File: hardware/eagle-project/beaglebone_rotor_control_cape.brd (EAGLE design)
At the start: 71.8 x 54.6 mm, 21 parts, among them IC1 TLC2264CDU, IC2 TLV5616, IC3 MAX3232ESE, Q1 SQ2348ES-T1-GE3, Q2 SQ2348ES-T1-GE3, X1 BEAGLEBONE_OUTLINE

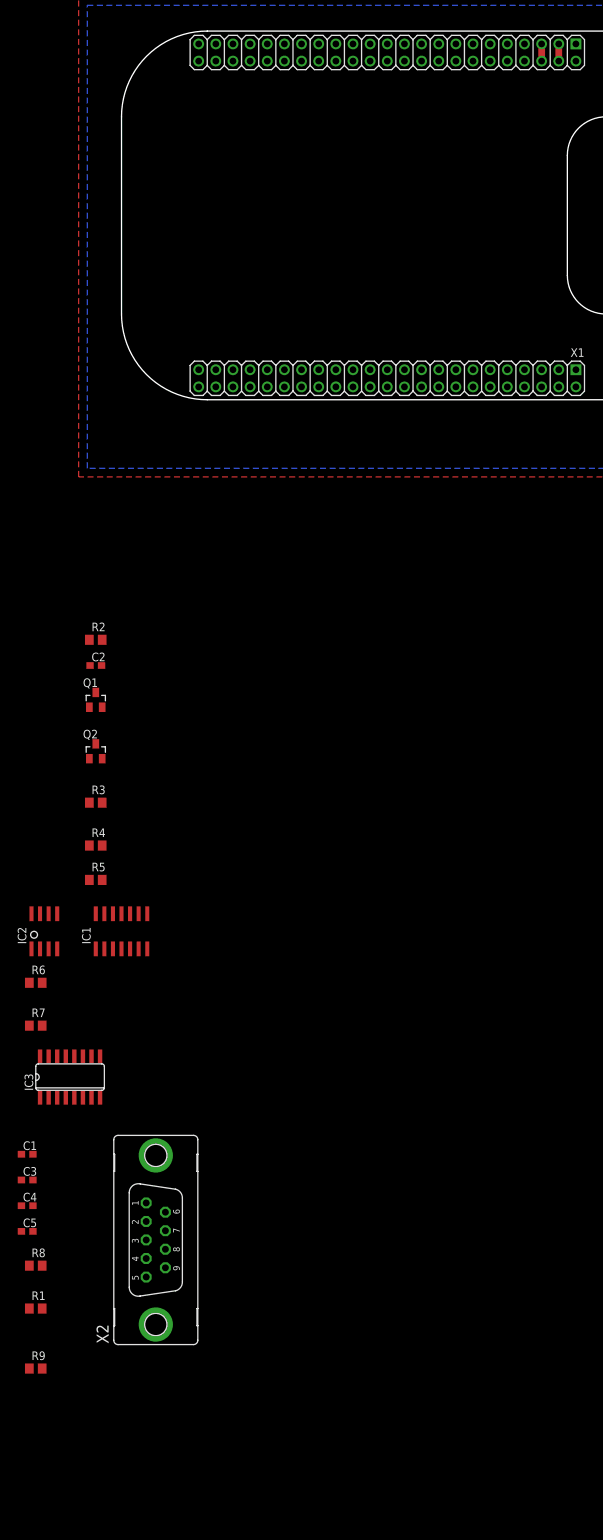
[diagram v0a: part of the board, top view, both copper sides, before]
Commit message: Eagle project update * RS232 rcv/drv layout done * AMP Press-Fit connector library created
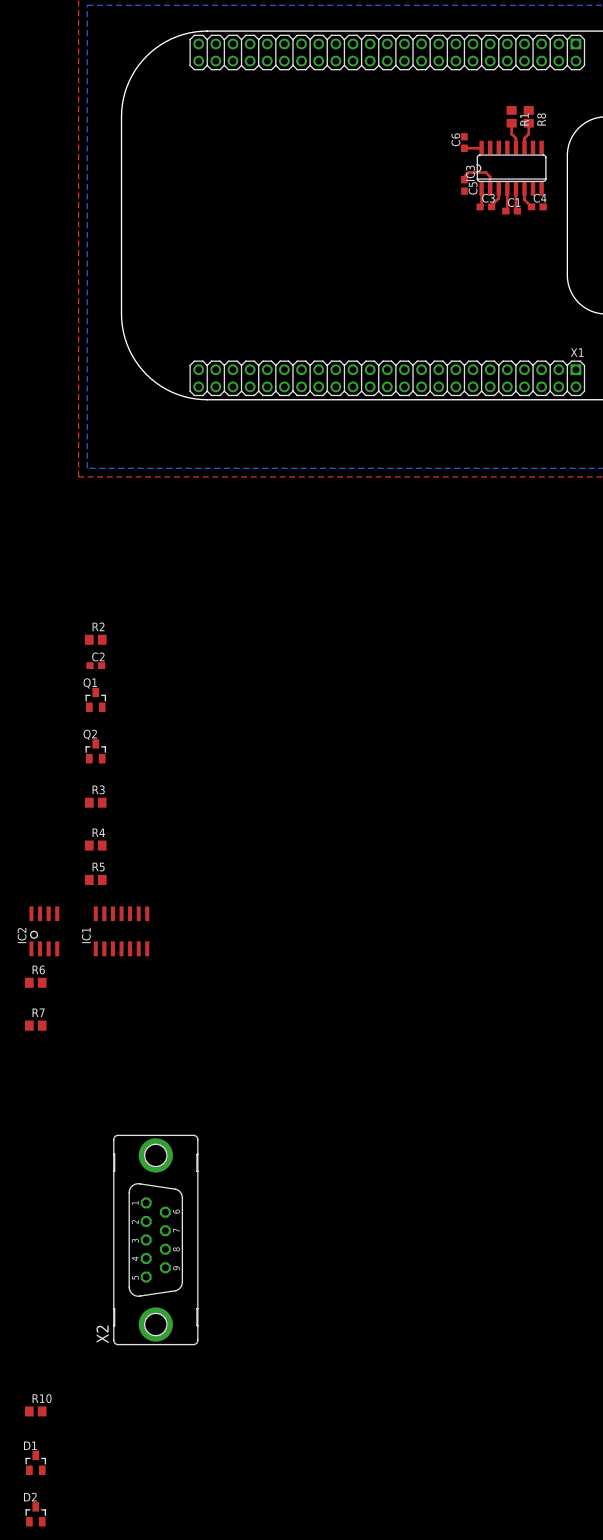
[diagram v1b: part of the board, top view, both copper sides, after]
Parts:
- removed R9: 15k, rcl:R0805
- added C6: 100n, rcl:C0603
- added D1: BAS40-04, diode:SOT23
- added D2: 5V1, diode:SOT23
- added R10: 10k, rcl:R0805
- R4: value (none) -> 10k
- R5: value (none) -> 5k6
- moved R1 190.1 mm to (59.1, 43.2), turned to 270 degrees
- moved R8 185.2 mm to (61.6, 43.2), turned to 270 degrees
- moved C5 167.9 mm to (52.1, 33.0), turned to 270 degrees
- moved C4 166.1 mm to (62.9, 29.8)
- moved C3 159.4 mm to (55.2, 29.8)
- moved C1 157.1 mm to (59.1, 29.2)
- moved IC3 149.7 mm to (59.1, 35.6)
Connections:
- removed net N$23: R1.1
- removed net N$24: R8.1
- removed net N$26: IC3.14
- removed net N$27: IC3.13
- removed net VCC: IC3.16
- removed net VDD_3V3EXP: X1.49, X1.50
- removed net VDD_5V: X1.51, X1.52
- new net +3V3: C6.1, IC3.16, X1.49, X1.50
- new net BB_UART4_RX: R1.1, X1.57
- new net BB_UART4_TX: R8.1, X1.59
- new net N$28: R10.2
- new net RS232_RX: IC3.13, X2.3
- new net RS232_TX: IC3.14, X2.2
- net +5V: now also D1.2, X1.51, X1.52
- net GND: now also C6.2, D1.1, D2.1, X2.5; no longer R9.1
- net N$12: now also D1.3, D2.3, R10.1; no longer R9.2
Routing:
- net N$21: track 0.00 -> 6.56 mm
- net N$25: track 0.00 -> 3.86 mm
- net N$22: track 0.00 -> 3.86 mm
- net N$17: track 0.00 -> 3.37 mm
- net N$16: track 0.00 -> 3.37 mm
- net N$20: track 0.00 -> 3.08 mm
- net N$18: track 0.00 -> 3.08 mm
- net N$19: track 0.00 -> 2.73 mm
- net +3V3: track 0.00 -> 2.59 mm
- net VDD_5V: track 2.54 -> 0.00 mm
- net VDD_3V3EXP: track 2.54 -> 0.00 mm

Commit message: Updated available components list
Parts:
- added C7: 100n, rcl:C0603
- added R9: 100, rcl:R0805
- C2: value (none) -> 100n
- moved R6 98.4 mm to (-12.1, -183.5)
- moved R7 85.7 mm to (-12.1, -177.2)
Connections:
- net N$28 renamed ROT_H_POSITON
- net N$3 renamed ROT_H_LEFT
- net N$6 renamed ROT_H_RIGHT
- removed net N$10: IC2.6
- new net ROT_H_SPEED: R9.2
- net +5V: now also C7.1, IC2.6
- net GND: now also C7.2
- net N$11: now also R7.2; no longer R7.1
- net N$13: now also R6.2; no longer R6.1
- net N$14: now also R7.1; no longer R7.2
- net N$15: now also R6.1; no longer R6.2
- net N$5: now also R9.1
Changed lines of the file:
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@@
 <elements>
 <element name="X1" library="beaglebone" package="BEAGLEBONE_SHIELD" value="BEAGLEBONE_OUTLINE" x="87.63" y="1.27" rot="R90"/>
-<element name="C2" library="rcl" package="C0603" value="" x="-2.54" y="-38.1"/>
+<element name="C2" library="rcl" package="C0603" value="100n" x="-2.54" y="-38.1"/>
 <element name="R2" library="rcl" package="R0805" value="1M" x="-2.54" y="-34.29"/>
 <element name="Q1" library="vishay_sq2348eS-t1-ge3" package="SOT23" value="SQ2348ES-T1-GE3" x="-2.54" y="-43.18"/>
@@
 <element name="IC1" library="ti-tlc2264cd" package="SO14" value="TLC2264CDU" x="1.27" y="-77.47"/>
 <element name="IC2" library="ti-tlv5616" package="SO08" value="TLV5616" x="-10.16" y="-77.47"/>
-<element name="R6" library="rcl" package="R0805" value="100" x="-11.43" y="-85.09"/>
-<element name="R7" library="rcl" package="R0805" value="100" x="-11.43" y="-91.44"/>
 <element name="IC3" library="maxim" package="SO16" value="MAX3232ESE" x="59.055" y="35.56">
 <attribute name="OC_NEWARK" value="79C3880" x="59.055" y="35.56" size="1.778" layer="27" display="off"/>
@@
 <element name="D2" library="diode" package="SOT23" value="5V1" x="-11.43" y="-163.83"/>
 <element name="C6" library="rcl" package="C0603" value="100n" x="52.07" y="39.37" rot="R90"/>
+<element name="R9" library="rcl" package="R0805" value="100" x="-12.065" y="-170.815"/>
+<element name="R7" library="rcl" package="R0805" value="100" x="-12.065" y="-177.165"/>
+<element name="R6" library="rcl" package="R0805" value="100" x="-12.065" y="-183.515"/>
+<element name="C7" library="rcl" package="C0603" value="100n" x="-12.7" y="-189.23"/>
 </elements>
 <signals>
@@
 <contactref element="C6" pad="2"/>
 <contactref element="X2" pad="5"/>
+<contactref element="C7" pad="2"/>
+<wire x1="-12.38" y1="-164.93" x2="-11.85" y2="-189.23" width="0" layer="19" extent="1-1"/>
 <wire x1="-12.38" y1="-157.31" x2="-12.38" y2="-164.93" width="0" layer="19" extent="1-1"/>
 <wire x1="4.9276" y1="-128.6764" x2="-12.38" y2="-157.31" width="0" layer="19" extent="1-1"/>
@@
 <wire x1="-3.49" y1="-34.29" x2="-1.69" y2="-38.1" width="0" layer="19" extent="1-1"/>
 <wire x1="68.58" y1="3.175" x2="-3.49" y2="-34.29" width="0" layer="19" extent="1-1"/>
-</signal>
-<signal name="N$3">
+<wire x1="68.58" y1="5.715" x2="68.58" y2="3.175" width="0" layer="19" extent="1-1"/>
+<wire x1="63.715" y1="29.845" x2="68.58" y2="5.715" width="0" layer="19" extent="1-1"/>
+<wire x1="55.88" y1="38.6334" x2="63.715" y2="29.845" width="0" layer="19" extent="1-1"/>
+<wire x1="52.07" y1="40.22" x2="55.88" y2="38.6334" width="0" layer="19" extent="1-1"/>
+<wire x1="52.07" y1="32.17" x2="55.88" y2="38.6334" width="0" layer="19" extent="1-1"/>
+<wire x1="68.58" y1="51.435" x2="55.88" y2="38.6334" width="0" layer="19" extent="1-1"/>
+<wire x1="68.58" y1="53.975" x2="68.58" y2="51.435" width="0" layer="19" extent="1-1"/>
+<wire x1="15.24" y1="51.435" x2="52.07" y2="40.22" width="0" layer="19" extent="1-1"/>
+<wire x1="15.24" y1="53.975" x2="15.24" y2="51.435" width="0" layer="19" extent="1-1"/>
+<wire x1="12.7" y1="53.975" x2="15.24" y2="53.975" width="0" layer="19" extent="1-1"/>
+<wire x1="12.7" y1="51.435" x2="15.24" y2="51.435" width="0" layer="19" extent="1-1"/>
+</signal>
+<signal name="ROT_H_LEFT">
 <contactref element="Q1" pad="3"/>
 </signal>
-<signal name="N$6">
+<signal name="ROT_H_RIGHT">
 <contactref element="Q2" pad="3"/>
 </signal>
@@
 <contactref element="X1" pad="51"/>
 <contactref element="X1" pad="52"/>
+<contactref element="C7" pad="1"/>
+<contactref element="IC2" pad="6"/>
+<wire x1="-10.48" y1="-157.31" x2="-13.55" y2="-189.23" width="0" layer="19" extent="1-1"/>
 <wire x1="1.27" y1="-80.07" x2="-10.48" y2="-157.31" width="0" layer="19" extent="1-1"/>
-<wire x1="-12.065" y1="-74.87" x2="1.27" y2="-80.07" width="0" layer="19" extent="1-1"/>
+<wire x1="-9.525" y1="-74.87" x2="1.27" y2="-80.07" width="0" layer="19" extent="1-1"/>
+<wire x1="-12.065" y1="-74.87" x2="-9.525" y2="-74.87" width="0" layer="19" extent="1-1"/>
 <wire x1="63.5" y1="51.435" x2="1.27" y2="-80.07" width="0" layer="19" extent="1-1"/>
 <wire x1="63.5" y1="53.975" x2="63.5" y2="51.435" width="0" layer="19" extent="1-1"/>
@@
 <contactref element="IC1" pad="1"/>
 <contactref element="IC1" pad="2"/>
+<contactref element="R9" pad="1"/>
+<wire x1="-2.54" y1="-80.07" x2="-13.015" y2="-170.815" width="0" layer="19" extent="1-1"/>
 <wire x1="-1.27" y1="-80.07" x2="-2.54" y2="-80.07" width="0" layer="19" extent="1-1"/>
 </signal>
@@
 <signal name="N$9">
 <contactref element="IC2" pad="4"/>
-</signal>
-<signal name="N$10">
-<contactref element="IC2" pad="6"/>
 </signal>
 <signal name="N$12">
@@
 <contactref element="R3" pad="2"/>
 <contactref element="Q2" pad="1"/>
-<contactref element="R7" pad="1"/>
-<wire x1="-1.59" y1="-58.42" x2="-12.38" y2="-91.44" width="0" layer="19" extent="1-1"/>
+<contactref element="R7" pad="2"/>
+<wire x1="-1.59" y1="-58.42" x2="-11.115" y2="-177.165" width="0" layer="19" extent="1-1"/>
 <wire x1="-3.49" y1="-51.9" x2="-1.59" y2="-58.42" width="0" layer="19" extent="1-1"/>
 </signal>
@@
 <contactref element="R2" pad="2"/>
 <contactref element="Q1" pad="1"/>
-<contactref element="R6" pad="1"/>
-<wire x1="-3.49" y1="-44.28" x2="-12.38" y2="-85.09" width="0" layer="19" extent="1-1"/>
+<contactref element="R6" pad="2"/>
+<wire x1="-3.49" y1="-44.28" x2="-11.115" y2="-183.515" width="0" layer="19" extent="1-1"/>
 <wire x1="-1.59" y1="-34.29" x2="-3.49" y2="-44.28" width="0" layer="19" extent="1-1"/>
-</signal>
-<signal name="N$14">
-<contactref element="R7" pad="2"/>
-</signal>
-<signal name="N$15">
-<contactref element="R6" pad="2"/>
 </signal>
 <signal name="N$16">
@@
 <wire x1="58.42" y1="38.6334" x2="4.9276" y2="-123.19" width="0" layer="19" extent="1-1"/>
 </signal>
-<signal name="N$28">
+<signal name="ROT_H_POSITON">
 <contactref element="R10" pad="2"/>
 </signal>
@@
 <wire x1="61.595" y1="44.13" x2="53.34" y2="53.975" width="0" layer="19" extent="1-1"/>
 </signal>
+<signal name="ROT_H_SPEED">
+<contactref element="R9" pad="2"/>
+</signal>
+<signal name="N$14">
+<contactref element="R7" pad="1"/>
+</signal>
+<signal name="N$15">
+<contactref element="R6" pad="1"/>
+</signal>
 </signals>

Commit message: Changed DAC from TI TLV5616 to Microchip MCP4901
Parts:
- IC2: value TLV5616 -> MCP4901; device ti-tlv5616:SO08 -> microchip_mcp4901:SO-08
- moved IC2 110.1 mm to (-17.8, -187.3)
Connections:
- removed net N$8: IC2.1
- new net N$7: IC2.5
- net +5V: now also IC2.1; no longer IC2.8
- net GND: now also IC2.7; no longer IC2.5
- net N$2: now also IC2.8; no longer IC2.7
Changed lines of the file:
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@@
 <element name="R5" library="rcl" package="R0805" value="5k6" x="-2.54" y="-69.85"/>
 <element name="IC1" library="ti-tlc2264cd" package="SO14" value="TLC2264CDU" x="1.27" y="-77.47"/>
-<element name="IC2" library="ti-tlv5616" package="SO08" value="TLV5616" x="-10.16" y="-77.47"/>
 <element name="IC3" library="maxim" package="SO16" value="MAX3232ESE" x="59.055" y="35.56">
 <attribute name="OC_NEWARK" value="79C3880" x="59.055" y="35.56" size="1.778" layer="27" display="off"/>
@@
 <element name="R6" library="rcl" package="R0805" value="100" x="-12.065" y="-183.515"/>
 <element name="C7" library="rcl" package="C0603" value="100n" x="-12.7" y="-189.23"/>
+<element name="IC2" library="microchip_mcp4901" package="SO-08" value="MCP4901" x="-17.78" y="-187.325"/>
 </elements>
 <signals>
@@
 <contactref element="C2" pad="2"/>
 <contactref element="IC1" pad="11"/>
-<contactref element="IC2" pad="5"/>
 <contactref element="IC3" pad="15"/>
 <contactref element="C4" pad="2"/>
@@
 <contactref element="X2" pad="5"/>
 <contactref element="C7" pad="2"/>
-<wire x1="-12.38" y1="-164.93" x2="-11.85" y2="-189.23" width="0" layer="19" extent="1-1"/>
+<contactref element="IC2" pad="7"/>
+<wire x1="-11.85" y1="-189.23" x2="-18.415" y2="-184.725" width="0" layer="19" extent="1-1"/>
+<wire x1="-12.38" y1="-164.93" x2="-18.415" y2="-184.725" width="0" layer="19" extent="1-1"/>
 <wire x1="-12.38" y1="-157.31" x2="-12.38" y2="-164.93" width="0" layer="19" extent="1-1"/>
 <wire x1="4.9276" y1="-128.6764" x2="-12.38" y2="-157.31" width="0" layer="19" extent="1-1"/>
 <wire x1="1.27" y1="-74.87" x2="4.9276" y2="-128.6764" width="0" layer="19" extent="1-1"/>
 <wire x1="-3.49" y1="-69.85" x2="1.27" y2="-74.87" width="0" layer="19" extent="1-1"/>
-<wire x1="-8.255" y1="-74.87" x2="-3.49" y2="-69.85" width="0" layer="19" extent="1-1"/>
 <wire x1="-3.49" y1="-58.42" x2="-3.49" y2="-69.85" width="0" layer="19" extent="1-1"/>
 <wire x1="-1.59" y1="-51.9" x2="-3.49" y2="-58.42" width="0" layer="19" extent="1-1"/>
@@
 <signal name="+5V">
 <contactref element="IC1" pad="4"/>
-<contactref element="IC2" pad="8"/>
 <contactref element="D1" pad="2"/>
 <contactref element="X1" pad="51"/>
 <contactref element="X1" pad="52"/>
 <contactref element="C7" pad="1"/>
+<contactref element="IC2" pad="1"/>
 <contactref element="IC2" pad="6"/>
-<wire x1="-10.48" y1="-157.31" x2="-13.55" y2="-189.23" width="0" layer="19" extent="1-1"/>
+<wire x1="-17.145" y1="-184.725" x2="-19.685" y2="-189.925" width="0" layer="19" extent="1-1"/>
+<wire x1="-13.55" y1="-189.23" x2="-17.145" y2="-184.725" width="0" layer="19" extent="1-1"/>
+<wire x1="-10.48" y1="-157.31" x2="-17.145" y2="-184.725" width="0" layer="19" extent="1-1"/>
 <wire x1="1.27" y1="-80.07" x2="-10.48" y2="-157.31" width="0" layer="19" extent="1-1"/>
-<wire x1="-9.525" y1="-74.87" x2="1.27" y2="-80.07" width="0" layer="19" extent="1-1"/>
-<wire x1="-12.065" y1="-74.87" x2="-9.525" y2="-74.87" width="0" layer="19" extent="1-1"/>
 <wire x1="63.5" y1="51.435" x2="1.27" y2="-80.07" width="0" layer="19" extent="1-1"/>
 <wire x1="63.5" y1="53.975" x2="63.5" y2="51.435" width="0" layer="19" extent="1-1"/>
@@
 </signal>
 <signal name="N$2">
-<contactref element="IC2" pad="7"/>
 <contactref element="IC1" pad="3"/>
-<wire x1="0" y1="-80.07" x2="-10.795" y2="-74.87" width="0" layer="19" extent="1-1"/>
-</signal>
-<signal name="N$4">
-<contactref element="IC2" pad="3"/>
-</signal>
-<signal name="N$7">
-<contactref element="IC2" pad="2"/>
-</signal>
-<signal name="N$8">
-<contactref element="IC2" pad="1"/>
-</signal>
-<signal name="N$9">
-<contactref element="IC2" pad="4"/>
+<contactref element="IC2" pad="8"/>
+<wire x1="0" y1="-80.07" x2="-19.685" y2="-184.725" width="0" layer="19" extent="1-1"/>
 </signal>
 <signal name="N$12">
@@
 <contactref element="R6" pad="1"/>
 </signal>
+<signal name="N$3">
+<contactref element="IC2" pad="2"/>
+</signal>
+<signal name="N$4">
+<contactref element="IC2" pad="3"/>
+</signal>
+<signal name="N$6">
+<contactref element="IC2" pad="4"/>
+</signal>
+<signal name="N$7">
+<contactref element="IC2" pad="5"/>
+</signal>
 </signals>

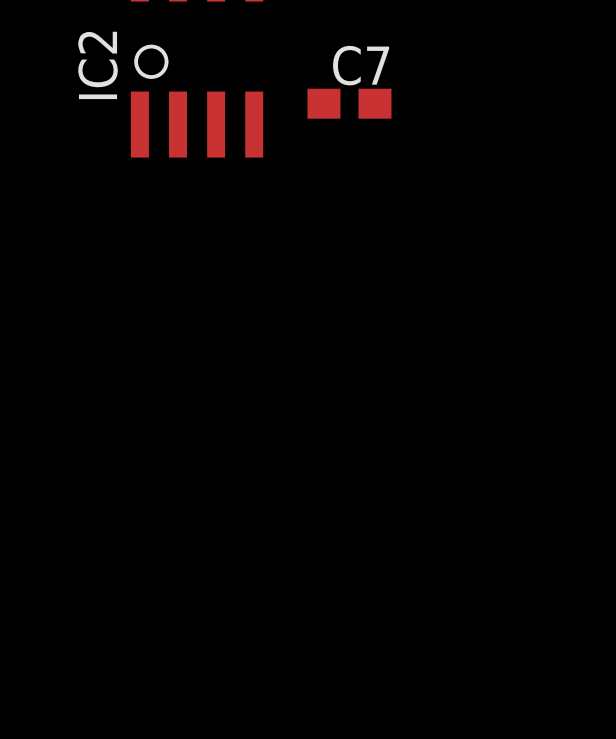
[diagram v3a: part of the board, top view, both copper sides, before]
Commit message: Added software draft for MCP4901 and some Eagle schematic updates
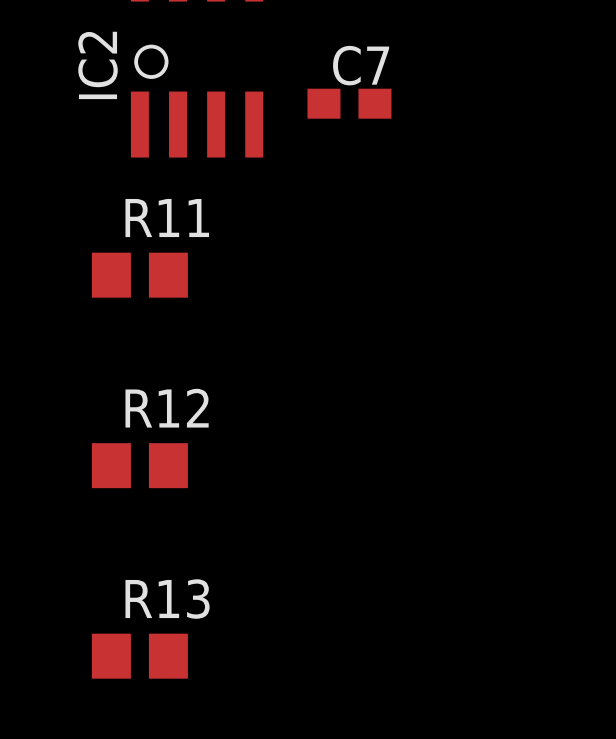
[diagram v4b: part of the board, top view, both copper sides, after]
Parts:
- added R11: 0, rcl:R0805
- added R12: 5k, rcl:R0805
- added R13: 10k, rcl:R0805
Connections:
- removed net N$4: IC2.3
- removed net N$6: IC2.4
- new net BB_SPI0_CS0: IC2.2, X1.63
- new net BB_SPI0_D0: IC2.4, X1.67
- new net BB_SPI0_D1: X1.64
- new net BB_SPI0_SCLK: IC2.3, X1.68
- net GND: now also R11.1, R13.1
- net N$3: now also IC1.1, R12.2, R9.1; no longer IC2.2
- net N$5: now also R12.1, R13.2; no longer IC1.1, R9.1
- net N$7: now also R11.2
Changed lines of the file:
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@@
 <element name="C7" library="rcl" package="C0603" value="100n" x="-12.7" y="-189.23"/>
 <element name="IC2" library="microchip_mcp4901" package="SO-08" value="MCP4901" x="-17.78" y="-187.325"/>
+<element name="R11" library="rcl" package="R0805" value="0" x="-19.685" y="-194.945"/>
+<element name="R12" library="rcl" package="R0805" value="5k" x="-19.685" y="-201.295"/>
+<element name="R13" library="rcl" package="R0805" value="10k" x="-19.685" y="-207.645"/>
 </elements>
 <signals>
@@
 <contactref element="C7" pad="2"/>
 <contactref element="IC2" pad="7"/>
+<contactref element="R11" pad="1"/>
+<contactref element="R13" pad="1"/>
+<wire x1="-20.635" y1="-194.945" x2="-20.635" y2="-207.645" width="0" layer="19" extent="1-1"/>
+<wire x1="-18.415" y1="-184.725" x2="-20.635" y2="-194.945" width="0" layer="19" extent="1-1"/>
 <wire x1="-11.85" y1="-189.23" x2="-18.415" y2="-184.725" width="0" layer="19" extent="1-1"/>
 <wire x1="-12.38" y1="-164.93" x2="-18.415" y2="-184.725" width="0" layer="19" extent="1-1"/>
@@
 </signal>
 <signal name="N$5">
-<contactref element="IC1" pad="1"/>
 <contactref element="IC1" pad="2"/>
-<contactref element="R9" pad="1"/>
-<wire x1="-2.54" y1="-80.07" x2="-13.015" y2="-170.815" width="0" layer="19" extent="1-1"/>
-<wire x1="-1.27" y1="-80.07" x2="-2.54" y2="-80.07" width="0" layer="19" extent="1-1"/>
+<contactref element="R12" pad="1"/>
+<contactref element="R13" pad="2"/>
+<wire x1="-20.635" y1="-201.295" x2="-18.735" y2="-207.645" width="0" layer="19" extent="1-1"/>
+<wire x1="-1.27" y1="-80.07" x2="-20.635" y2="-201.295" width="0" layer="19" extent="1-1"/>
 </signal>
 <signal name="N$2">
@@
 <contactref element="R6" pad="1"/>
 </signal>
-<signal name="N$3">
-<contactref element="IC2" pad="2"/>
-</signal>
-<signal name="N$4">
-<contactref element="IC2" pad="3"/>
-</signal>
-<signal name="N$6">
-<contactref element="IC2" pad="4"/>
-</signal>
 <signal name="N$7">
 <contactref element="IC2" pad="5"/>
+<contactref element="R11" pad="2"/>
+<wire x1="-15.875" y1="-184.725" x2="-18.735" y2="-194.945" width="0" layer="19" extent="1-1"/>
+</signal>
+<signal name="BB_SPI0_CS0">
+<contactref element="X1" pad="63"/>
+<contactref element="IC2" pad="2"/>
+<wire x1="48.26" y1="53.975" x2="-18.415" y2="-189.925" width="0" layer="19" extent="1-1"/>
+</signal>
+<signal name="BB_SPI0_D1">
+<contactref element="X1" pad="64"/>
+</signal>
+<signal name="BB_SPI0_D0">
+<contactref element="X1" pad="67"/>
+<contactref element="IC2" pad="4"/>
+<wire x1="43.18" y1="53.975" x2="-15.875" y2="-189.925" width="0" layer="19" extent="1-1"/>
+</signal>
+<signal name="BB_SPI0_SCLK">
+<contactref element="X1" pad="68"/>
+<contactref element="IC2" pad="3"/>
+<wire x1="43.18" y1="51.435" x2="-17.145" y2="-189.925" width="0" layer="19" extent="1-1"/>
+</signal>
+<signal name="N$3">
+<contactref element="IC1" pad="1"/>
+<contactref element="R9" pad="1"/>
+<contactref element="R12" pad="2"/>
+<wire x1="-13.015" y1="-170.815" x2="-18.735" y2="-201.295" width="0" layer="19" extent="1-1"/>
+<wire x1="-2.54" y1="-80.07" x2="-13.015" y2="-170.815" width="0" layer="19" extent="1-1"/>
 </signal>
 </signals>
